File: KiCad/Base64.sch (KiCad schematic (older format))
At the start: 2 parts, among them J1 1473149-1, U1 68000D

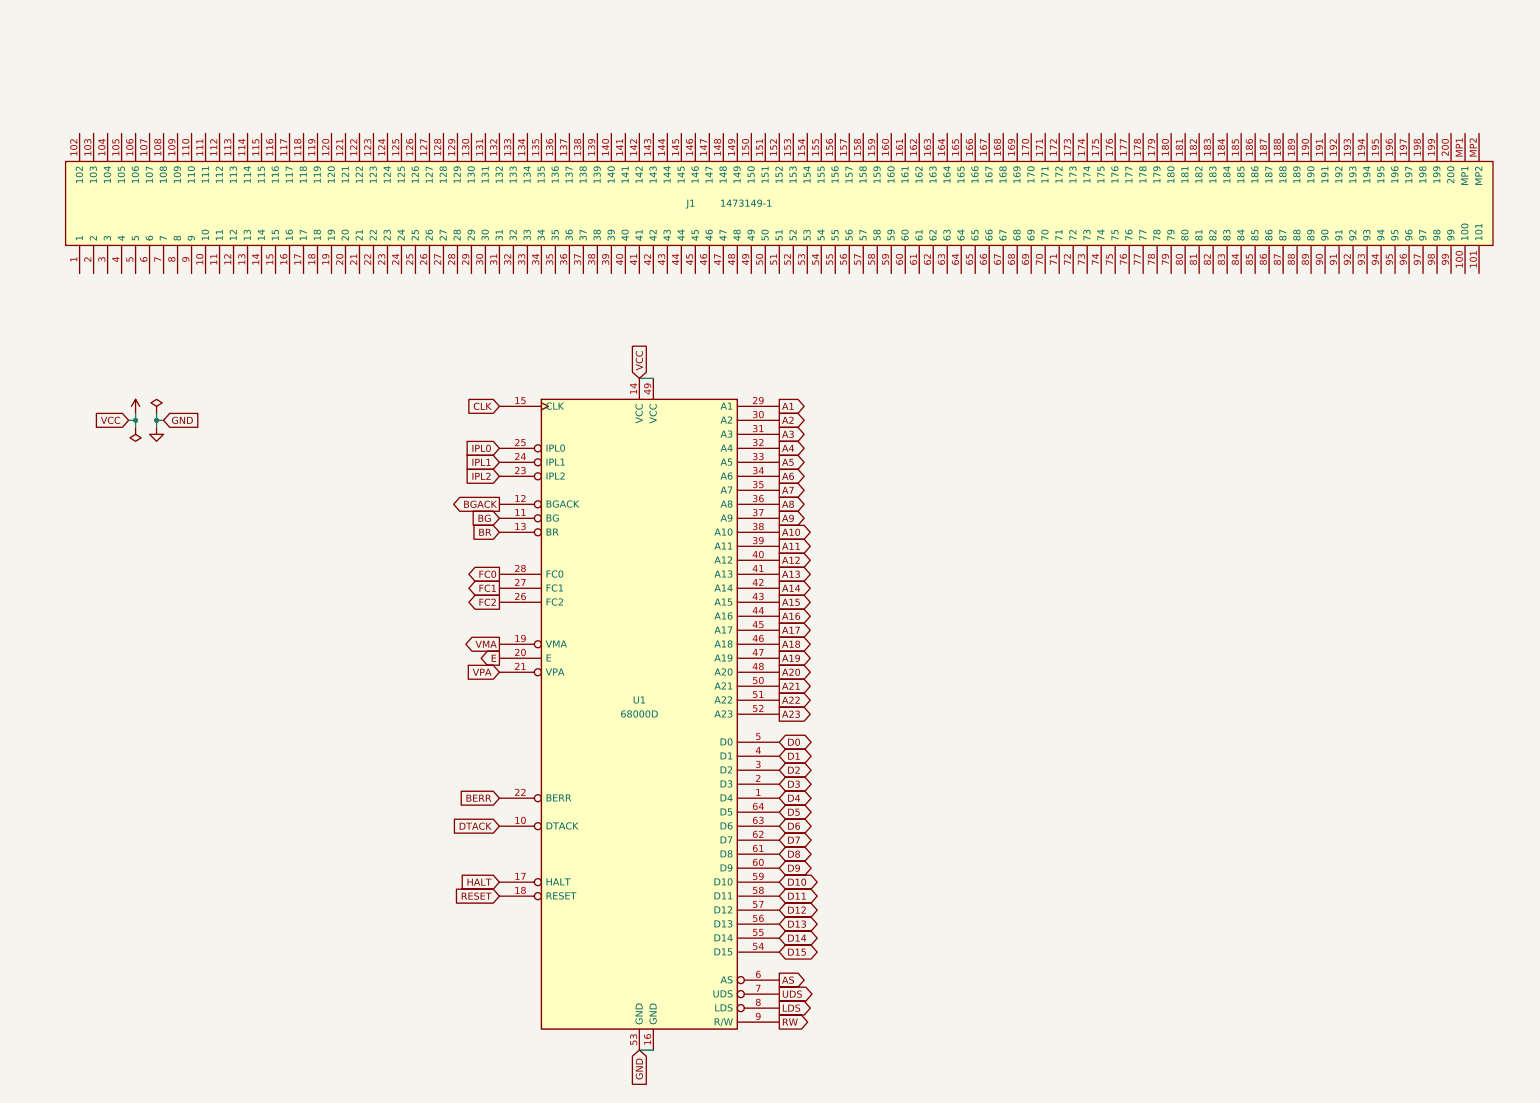
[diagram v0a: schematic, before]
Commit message: more placement and routing
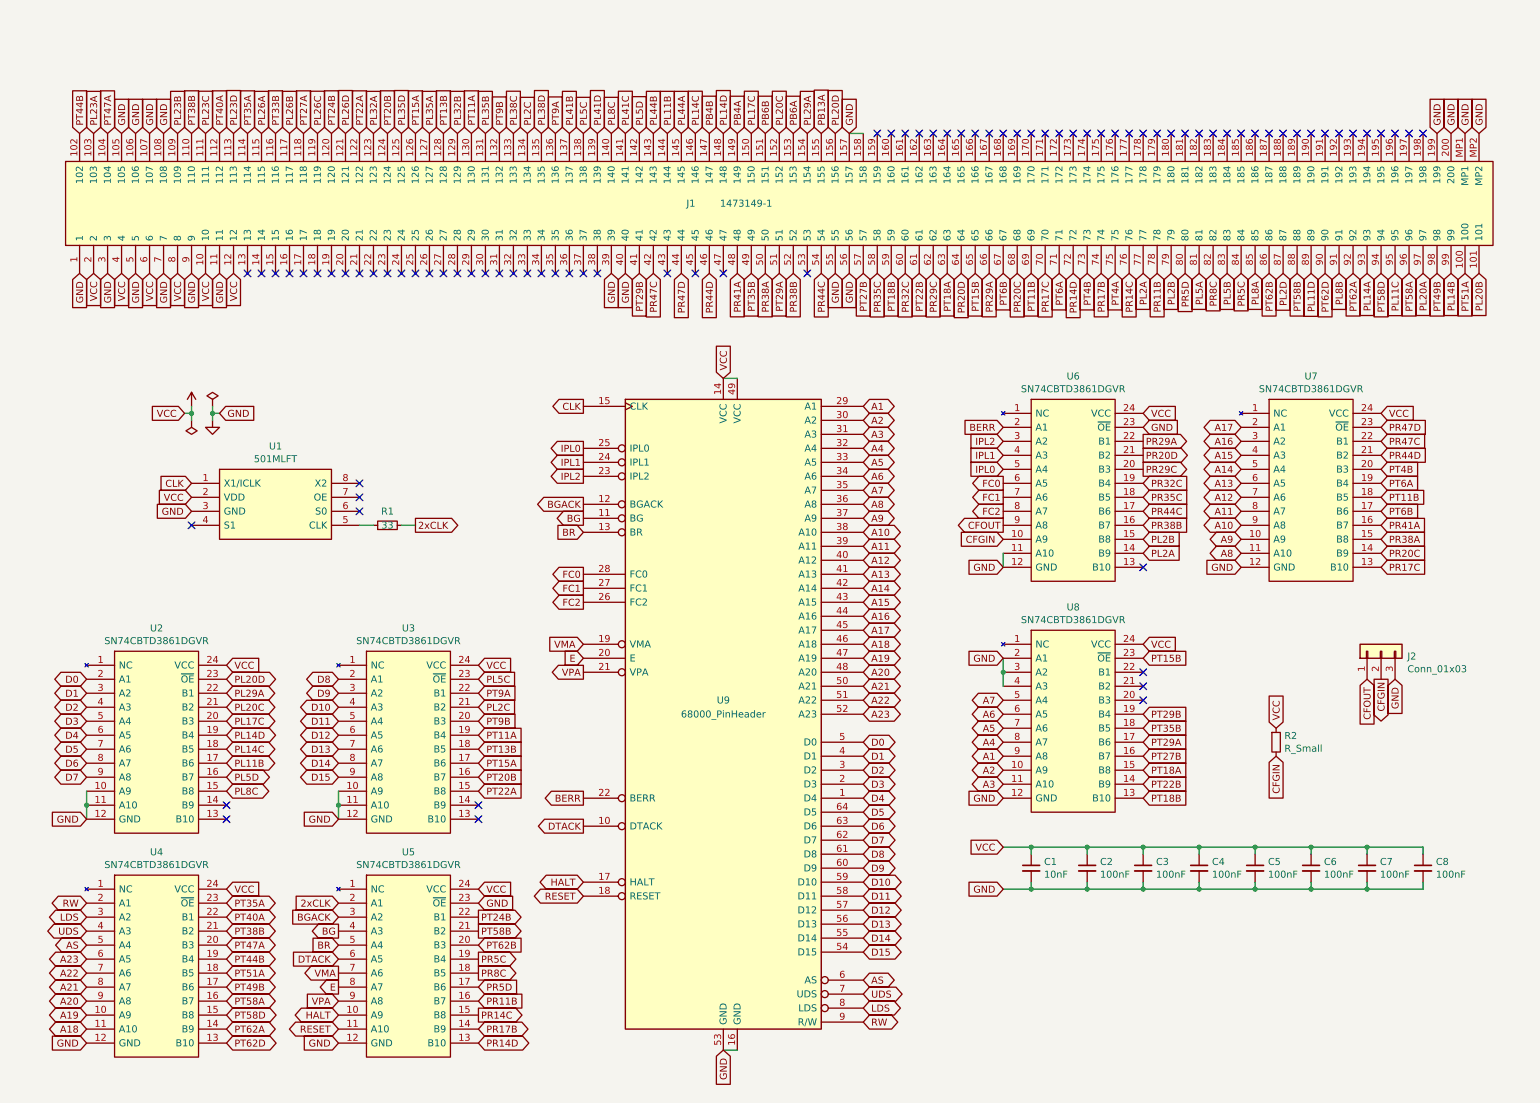
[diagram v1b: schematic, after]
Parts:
- added C1: 10nF, Capacitor_SMD:C_0603_1608Metric, symbol Device:C_Small
- added C2, C3, C4, C5, C6, C7, C8: 100nF, Capacitor_SMD:C_0603_1608Metric, symbol Device:C_Small
- added J2: Conn_01x03, Connector_PinHeader_2.54mm:PinHeader_1x03_P2.54mm_Horizontal, symbol Connector_Generic:Conn_01x03
- added R1: 33, Resistor_SMD:R_0603_1608Metric, symbol Device:R_Small
- added R2: R_Small, Resistor_SMD:R_0603_1608Metric, symbol Device:R_Small
- added U1: 501MLFT, Package_SO:SOIC-8_3.9x4.9mm_P1.27mm, symbol Base64:501MLFT
- added U2, U3, U4, U5, U6, U7, U8: SN74CBTD3861DGVR, Package_SO:TSSOP-24_4.4x5mm_P0.4mm, symbol Base64:SN74CBTD3861DGVR
- U9: renamed from U1; value 68000D -> 68000_PinHeader
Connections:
- net A1: now also U8.9 (A8)
- net A10: now also U7.9 (A8)
- net A11: now also U7.8 (A7)
- net A12: now also U7.7 (A6)
- net A13: now also U7.6 (A5)
- net A14: now also U7.5 (A4)
- net A15: now also U7.4 (A3)
- net A16: now also U7.3 (A2)
- net A17: now also U7.2 (A1)
- net A18: now also U4.11 (A10)
- net A19: now also U4.10 (A9)
- net A2: now also U8.10 (A9)
- net A20: now also U4.9 (A8)
- net A21: now also U4.8 (A7)
- net A22: now also U4.7 (A6)
- net A23: now also U4.6 (A5)
- net A3: now also U8.11 (A10)
- net A4: now also U8.8 (A7)
- net A5: now also U8.7 (A6)
- net A6: now also U8.6 (A5)
- net A7: now also U8.5 (A4)
- net A8: now also U7.11 (A10)
- net A9: now also U7.10 (A9)
- net AS: now also U4.5 (A4)
- net BERR: now also U6.2 (A1)
- net BG: now also U5.4 (A3)
- net BGACK: now also U5.3 (A2)
- net BR: now also U5.5 (A4)
- net CLK: now also U1.1 (X1/ICLK)
- net D0: now also U2.2 (A1)
- net D1: now also U2.3 (A2)
- net D10: now also U3.4 (A3)
- net D11: now also U3.5 (A4)
- net D12: now also U3.6 (A5)
- net D13: now also U3.7 (A6)
- net D14: now also U3.8 (A7)
- net D15: now also U3.9 (A8)
- net D2: now also U2.4 (A3)
- net D3: now also U2.5 (A4)
- net D4: now also U2.6 (A5)
- net D5: now also U2.7 (A6)
- net D6: now also U2.8 (A7)
- net D7: now also U2.9 (A8)
- net D8: now also U3.2 (A1)
- net D9: now also U3.3 (A2)
- net DTACK: now also U5.6 (A5)
- net E: now also U5.8 (A7)
- net FC0: now also U6.6 (A5)
- net FC1: now also U6.7 (A6)
- net FC2: now also U6.8 (A7)
- net GND: now also J1.1, J1.105, J1.106, J1.107, J1.108, J1.11, J1.157, J1.158, J1.199, J1.200, J1.3, J1.39, J1.40, J1.5, J1.55, J1.56, J1.7, J1.9, J1.MP1, J1.MP2, C1.2, C2.2, C3.2, C4.2, C5.2, C6.2, C7.2, C8.2, J2.3 (Pin_3), U1.3 (GND), U2.10 (A9), U2.11 (A10), U2.12 (GND), U3.10 (A9), U3.11 (A10), U3.12 (GND), U4.12 (GND), U5.12 (GND), U5.23 (~OE), U6.11 (A10), U6.12 (GND), U6.23 (~OE), U7.12 (GND), U8.12 (GND), U8.2 (A1), U8.3 (A2), U8.4 (A3)
- net HALT: now also U5.10 (A9)
- net IPL0: now also U6.5 (A4)
- net IPL1: now also U6.4 (A3)
- net IPL2: now also U6.3 (A2)
- net LDS: now also U4.3 (A2)
- net RESET: now also U5.11 (A10)
- net RW: now also U4.2 (A1)
- net UDS: now also U4.4 (A3)
- net VCC: now also J1.10, J1.12, J1.2, J1.4, J1.6, J1.8, C1.1, C2.1, C3.1, C4.1, C5.1, C6.1, C7.1, C8.1, R2.1, U1.2 (VDD), U2.24 (VCC), U3.24 (VCC), U4.24 (VCC), U5.24 (VCC), U6.24 (VCC), U7.24 (VCC), U8.24 (VCC)
- net VMA: now also U5.7 (A6)
- net VPA: now also U5.9 (A8)
- net PT51A: now reaches J1.100
- net PT51A: now also U4.18 (B5)
- net PL20B: now reaches J1.101
- net PT44B: now reaches J1.102
- net PT44B: now also U4.19 (B4)
- net PL23A: now reaches J1.103
- net PT47A: now reaches J1.104
- net PT47A: now also U4.20 (B3)
- net PL23B: now reaches J1.109
- net PT38B: now reaches J1.110
- net PT38B: now also U4.21 (B2)
- net PL23C: now reaches J1.111
- net PT40A: now reaches J1.112
- net PT40A: now also U4.22 (B1)
- net PL23D: now reaches J1.113
- net PT35A: now reaches J1.114
- net PT35A: now also U4.23 (~OE)
- net PL26A: now reaches J1.115
- net PT33B: now reaches J1.116
- net PL26B: now reaches J1.117
- net PT27A: now reaches J1.118
- net PL26C: now reaches J1.119
- net PT24B: now reaches J1.120
- net PT24B: now also U5.22 (B1)
- net PL26D: now reaches J1.121
- net PT22A: now reaches J1.122
- net PT22A: now also U3.15 (B8)
- net PL32A: now reaches J1.123
- net PT20B: now reaches J1.124
- net PT20B: now also U3.16 (B7)
- net PL35D: now reaches J1.125
- net PT15A: now reaches J1.126
- net PT15A: now also U3.17 (B6)
- net PL35A: now reaches J1.127
- net PT13B: now reaches J1.128
- net PT13B: now also U3.18 (B5)
- net PL32B: now reaches J1.129
- net PT11A: now reaches J1.130
- net PT11A: now also U3.19 (B4)
- net PL35B: now reaches J1.131
- net PT9B: now reaches J1.132
- net PT9B: now also U3.20 (B3)
- net PL38C: now reaches J1.133
- net PL2C: now reaches J1.134
- net PL2C: now also U3.21 (B2)
- net PL38D: now reaches J1.135
- net PT9A: now reaches J1.136
- net PT9A: now also U3.22 (B1)
- net PL41B: now reaches J1.137
- net PL5C: now reaches J1.138
- net PL5C: now also U3.23 (~OE)
- net PL41D: now reaches J1.139
- net PL8C: now reaches J1.140
- net PL8C: now also U2.15 (B8)
- net PL41C: now reaches J1.141
- net PL5D: now reaches J1.142
- net PL5D: now also U2.16 (B7)
- net PL44B: now reaches J1.143
- net PL11B: now reaches J1.144
- net PL11B: now also U2.17 (B6)
- net PL44A: now reaches J1.145
- net PL14C: now reaches J1.146
- net PL14C: now also U2.18 (B5)
- net PB4B: now reaches J1.147
- net PL14D: now reaches J1.148
- net PL14D: now also U2.19 (B4)
- net PB4A: now reaches J1.149
- net PL17C: now reaches J1.150
- net PL17C: now also U2.20 (B3)
- net PB6B: now reaches J1.151
- net PL20C: now reaches J1.152
- net PL20C: now also U2.21 (B2)
- net PB6A: now reaches J1.153
- net PL29A: now reaches J1.154
- net PL29A: now also U2.22 (B1)
- net PB13A: now reaches J1.155
- net PL20D: now reaches J1.156
- net PL20D: now also U2.23 (~OE)
- net PT29B: now reaches J1.41
- net PT29B: now also U8.19 (B4)
- net PR47C: now reaches J1.42
- net PR47C: now also U7.22 (B1)
- net PR47D: now reaches J1.44
- net PR47D: now also U7.23 (~OE)
- net PR44D: now reaches J1.46
- net PR44D: now also U7.21 (B2)
- net PR41A: now reaches J1.48
- net PR41A: now also U7.16 (B7)
- net PT35B: now reaches J1.49
- net PT35B: now also U8.18 (B5)
- net PR38A: now reaches J1.50
- net PR38A: now also U7.15 (B8)
- net PT29A: now reaches J1.51
- net PT29A: now also U8.17 (B6)
- net PR38B: now reaches J1.52
- net PR38B: now also U6.16 (B7)
- net PR44C: now reaches J1.54
- net PR44C: now also U6.17 (B6)
- net PT27B: now reaches J1.57
- net PT27B: now also U8.16 (B7)
- net PR35C: now reaches J1.58
- net PR35C: now also U6.18 (B5)
- net PT18B: now reaches J1.59
- net PT18B: now also U8.13 (B10)
- net PR32C: now reaches J1.60
- net PR32C: now also U6.19 (B4)
- net PT22B: now reaches J1.61
- net PT22B: now also U8.14 (B9)
- net PR29C: now reaches J1.62
- net PR29C: now also U6.20 (B3)
- net PT18A: now reaches J1.63
- net PT18A: now also U8.15 (B8)
- net PR20D: now reaches J1.64
- net PR20D: now also U6.21 (B2)
- net PT15B: now reaches J1.65
- net PT15B: now also U8.23 (~OE)
- net PR29A: now reaches J1.66
- net PR29A: now also U6.22 (B1)
- net PT6B: now reaches J1.67
- net PT6B: now also U7.17 (B6)
- net PR20C: now reaches J1.68
- net PR20C: now also U7.14 (B9)
- net PT11B: now reaches J1.69
- net PT11B: now also U7.18 (B5)
- net PR17C: now reaches J1.70
- net PR17C: now also U7.13 (B10)
- net PT6A: now reaches J1.71
- net PT6A: now also U7.19 (B4)
- net PR14D: now reaches J1.72
- net PR14D: now also U5.13 (B10)
- net PT4B: now reaches J1.73
- net PT4B: now also U7.20 (B3)
- net PR17B: now reaches J1.74
- net PR17B: now also U5.14 (B9)
- net PT4A: now reaches J1.75
- net PR14C: now reaches J1.76
- net PR14C: now also U5.15 (B8)
- net PL2A: now reaches J1.77
- net PL2A: now also U6.14 (B9)
- net PR11B: now reaches J1.78
- net PR11B: now also U5.16 (B7)
- net PL2B: now reaches J1.79
- net PL2B: now also U6.15 (B8)
- net PR5D: now reaches J1.80
- net PR5D: now also U5.17 (B6)
- net PL5A: now reaches J1.81
- net PR8C: now reaches J1.82
- net PR8C: now also U5.18 (B5)
- net PL5B: now reaches J1.83
- net PR5C: now reaches J1.84
- net PR5C: now also U5.19 (B4)
- net PL8A: now reaches J1.85
- net PT62B: now reaches J1.86
- net PT62B: now also U5.20 (B3)
- net PL2D: now reaches J1.87
- net PT58B: now reaches J1.88
- net PT58B: now also U5.21 (B2)
- net PL11D: now reaches J1.89
- net PT62D: now reaches J1.90
- net PT62D: now also U4.13 (B10)
- net PL8B: now reaches J1.91
- net PT62A: now reaches J1.92
- net PT62A: now also U4.14 (B9)
- net PL14A: now reaches J1.93
- net PT58D: now reaches J1.94
- net PT58D: now also U4.15 (B8)
- net PL11C: now reaches J1.95
- net PT58A: now reaches J1.96
- net PT58A: now also U4.16 (B7)
- net PL20A: now reaches J1.97
- net PT49B: now reaches J1.98
- net PT49B: now also U4.17 (B6)
- net PL14B: now reaches J1.99
- new net: R1.1, U1.5 (CLK)
- new net 2xCLK: R1.2, U5.2 (A1)
- new net CFGIN: J2.2 (Pin_2), R2.2, U6.10 (A9)
- new net CFOUT: J2.1 (Pin_1), U6.9 (A8)
- no-connect marks 0 -> 82
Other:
- moved on the sheet: U9

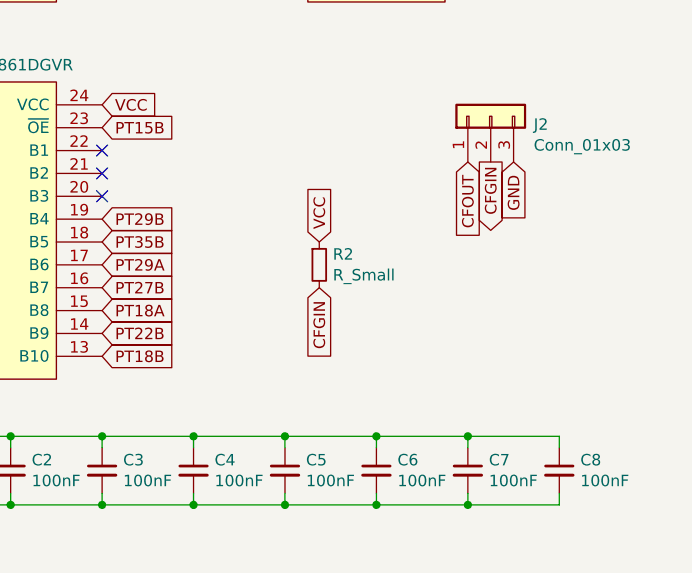
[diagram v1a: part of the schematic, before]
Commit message: Add value (10k) to R2 pull-up resistor and some small routing improvements
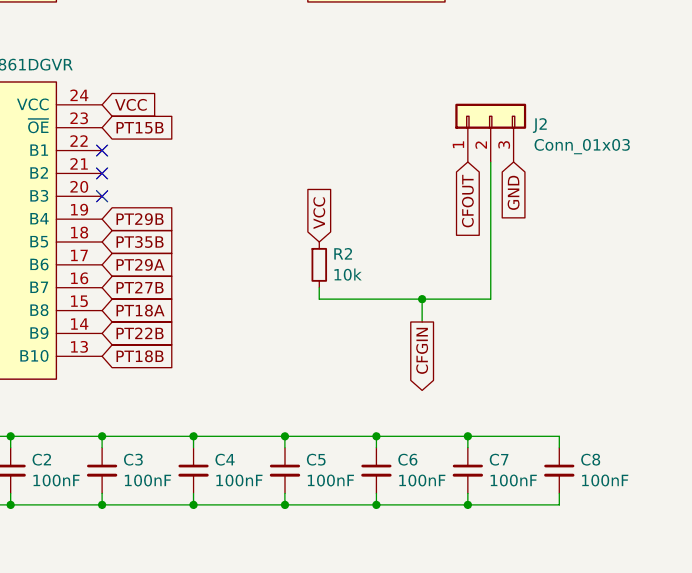
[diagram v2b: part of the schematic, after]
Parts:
- R2: value R_Small -> 10k
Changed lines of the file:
@@
 P 9450 5300
 F 0 "R2" H 9509 5346 50  0000 L CNN
-F 1 "R_Small" H 9509 5255 50  0000 L CNN
+F 1 "10k" H 9509 5255 50  0000 L CNN
 F 2 "Resistor_SMD:R_0603_1608Metric" H 9450 5300 50  0001 C CNN
 F 3 "~" H 9450 5300 50  0001 C CNN
@@
 Text GLabel 9450 5200 1    50   Input ~ 0
 VCC
-Text GLabel 9450 5400 3    50   Input ~ 0
-CFGIN
 Text GLabel 7500 4700 0    50   Input ~ 0
 GND
@@
 Text GLabel 10300 4850 3    50   Input ~ 0
 GND
-Text GLabel 10200 4850 3    50   Output ~ 0
+Text GLabel 9900 5550 3    50   Output ~ 0
 CFGIN
 Text GLabel 10100 4850 3    50   Input ~ 0
@@
 	950  5650 950  5750
 Connection ~ 950  5750
+Wire Wire Line
+	9450 5400 9450 5450
+Wire Wire Line
+	9450 5450 9900 5450
+Wire Wire Line
+	9900 5450 10200 5450
+Wire Wire Line
+	10200 5450 10200 4850
+Connection ~ 9900 5450
+Wire Wire Line
+	9900 5450 9900 5550
 $EndSCHEMATC

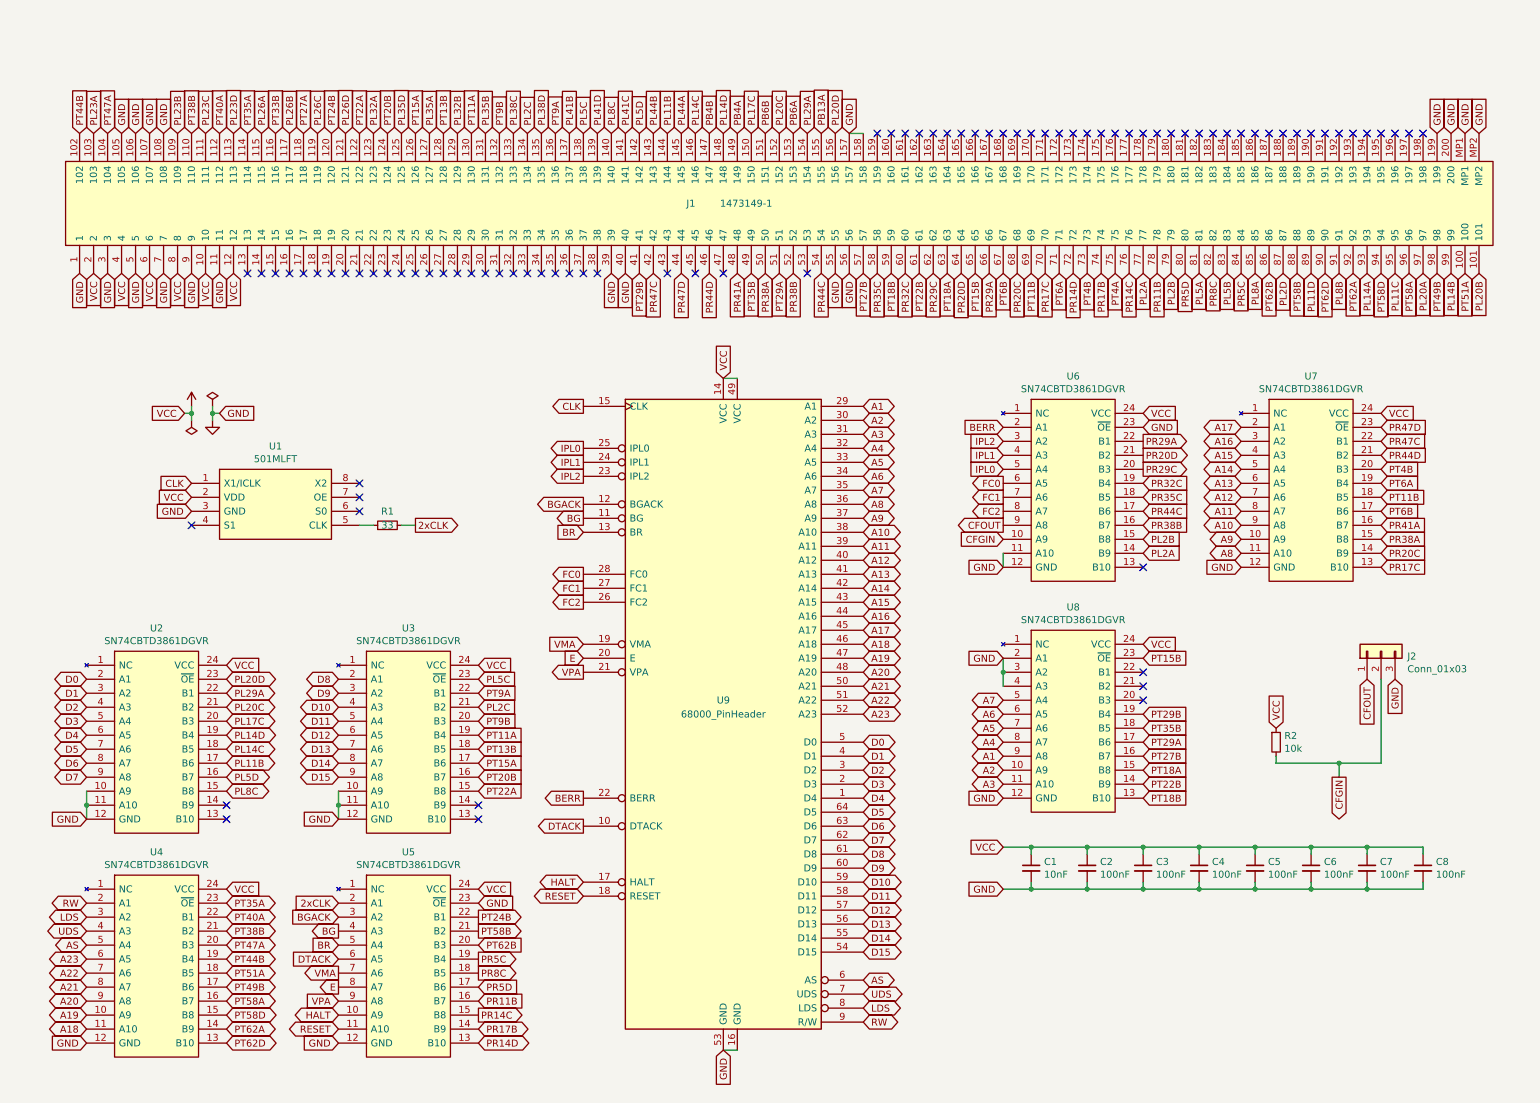
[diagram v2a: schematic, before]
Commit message: Fixed typo on CFGOUT net and corrected signal direction on many nets
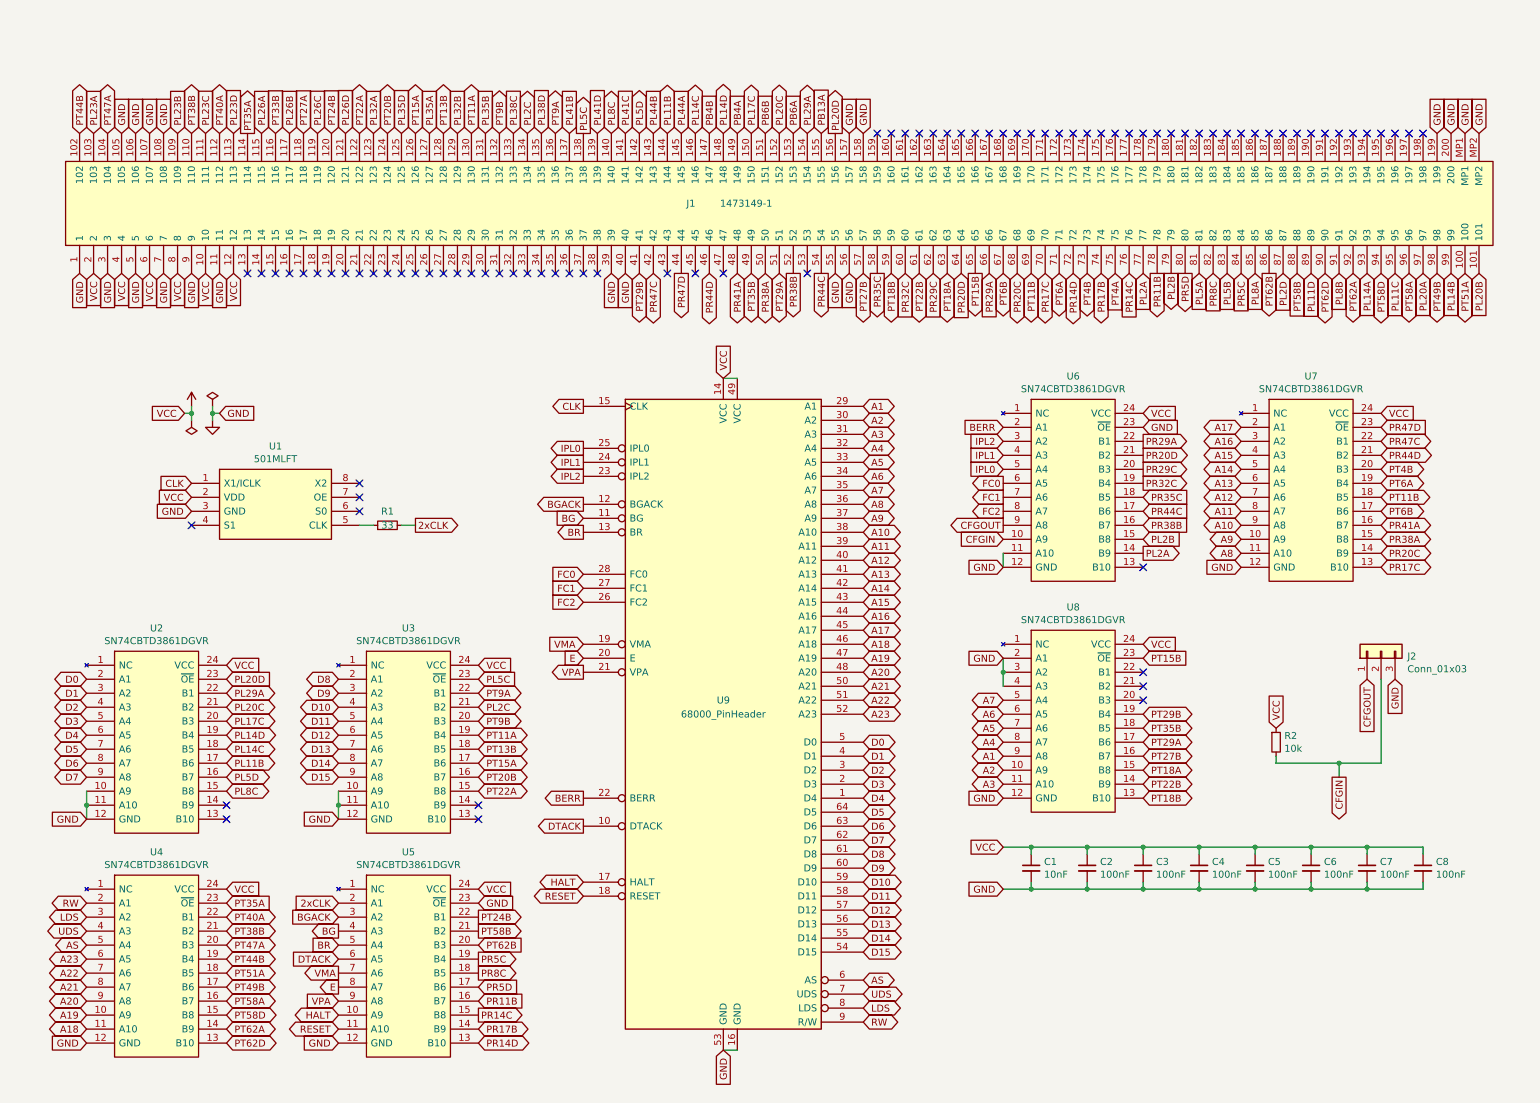
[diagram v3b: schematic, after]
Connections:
- net CFOUT renamed CFGOUT
